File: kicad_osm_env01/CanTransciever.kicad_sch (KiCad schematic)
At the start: 24 parts

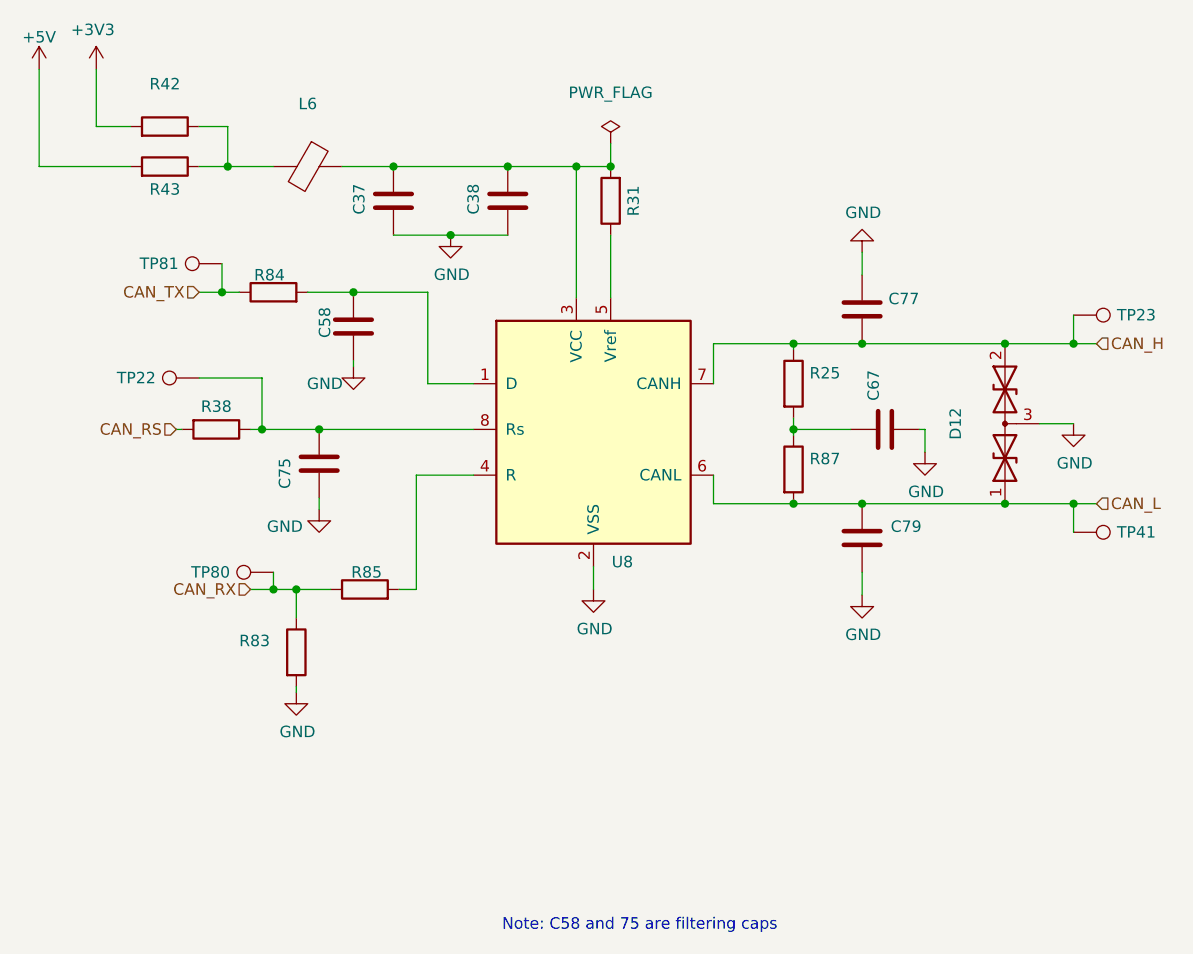
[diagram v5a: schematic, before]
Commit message: majority of signals routed on layout
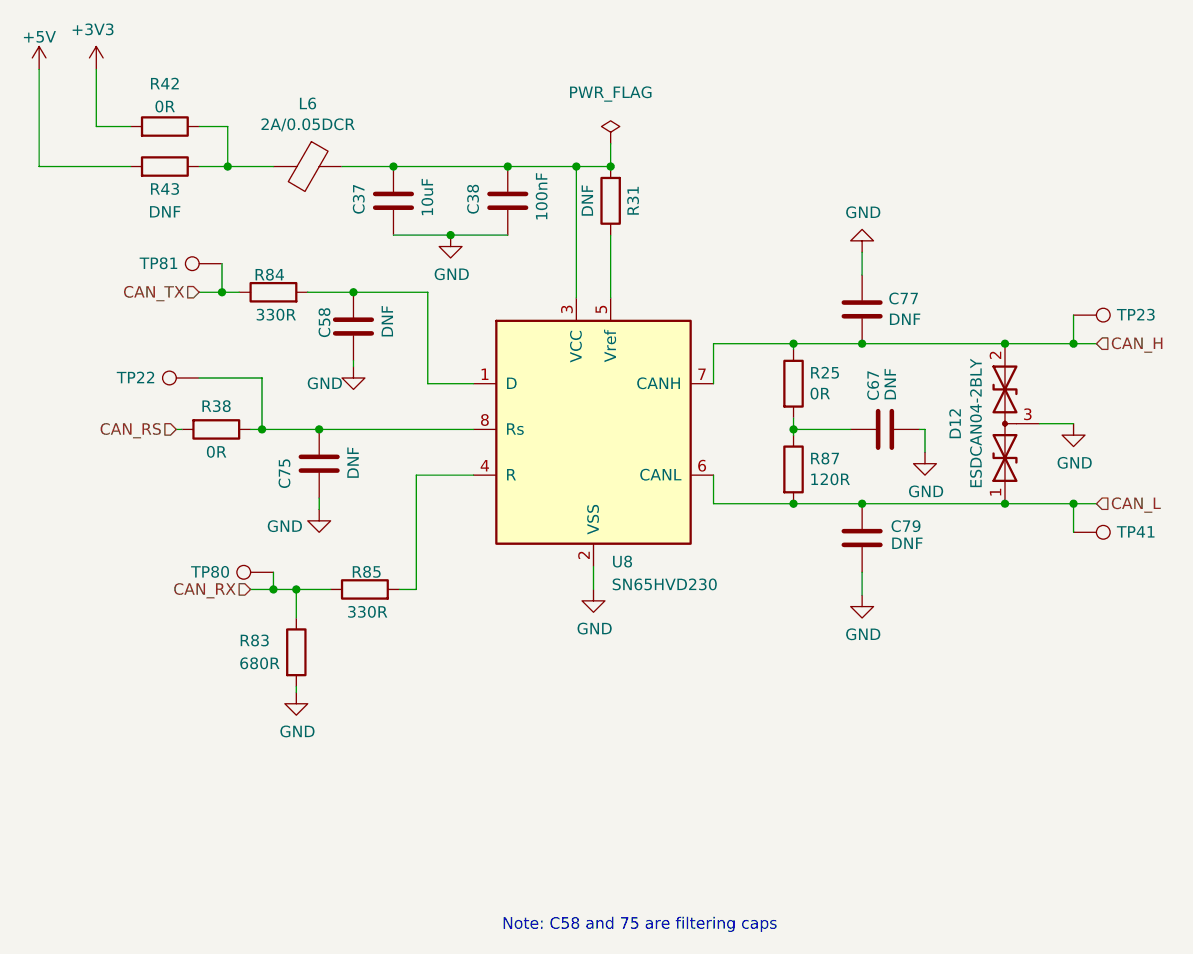
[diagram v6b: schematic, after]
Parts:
- C37: value (none) -> 10uF; footprint (none) -> Capacitor_SMD:C_0603_1608Metric
- C38: value (none) -> 100nF; footprint (none) -> Capacitor_SMD:C_0402_1005Metric
- C58, C67, C75, C77, C79: value (none) -> DNF; footprint (none) -> Capacitor_SMD:C_0603_1608Metric
- D12: value (none) -> ESDCAN04-2BLY; footprint (none) -> Package_TO_SOT_SMD:SOT-23
- L6: value (none) -> 2A/0.05DCR; footprint (none) -> Inductor_SMD:L_0402_1005Metric
- R25, R38, R42: value (none) -> 0R; footprint (none) -> Resistor_SMD:R_0603_1608Metric
- R31, R43: value (none) -> DNF; footprint (none) -> Resistor_SMD:R_0603_1608Metric
- R83: value (none) -> 680R; footprint (none) -> Resistor_SMD:R_0603_1608Metric
- R84, R85: value (none) -> 330R; footprint (none) -> Resistor_SMD:R_0603_1608Metric
- R87: value (none) -> 120R; footprint (none) -> Resistor_SMD:R_0603_1608Metric
- TP22, TP23, TP41, TP80, TP81: value (none) -> Test_Point; footprint (none) -> TestPoint:TestPoint_THTPad_D1.0mm_Drill0.5mm
- U8: value (none) -> SN65HVD230; footprint (none) -> Package_SO:SOIC-8_3.9x4.9mm_P1.27mm

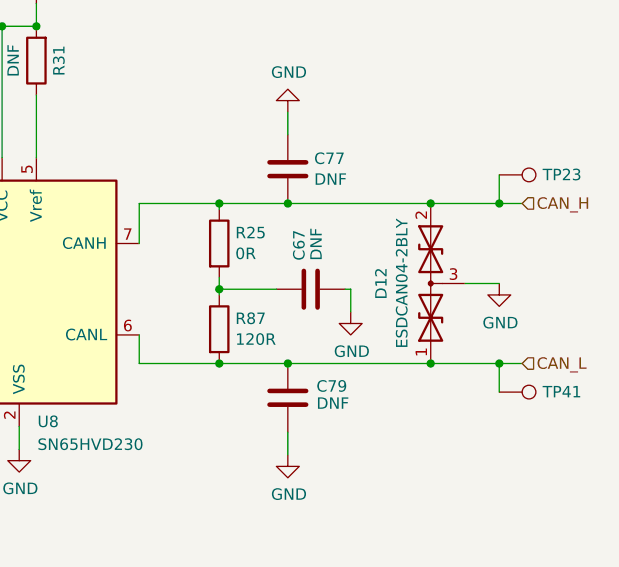
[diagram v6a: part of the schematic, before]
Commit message: updated layout
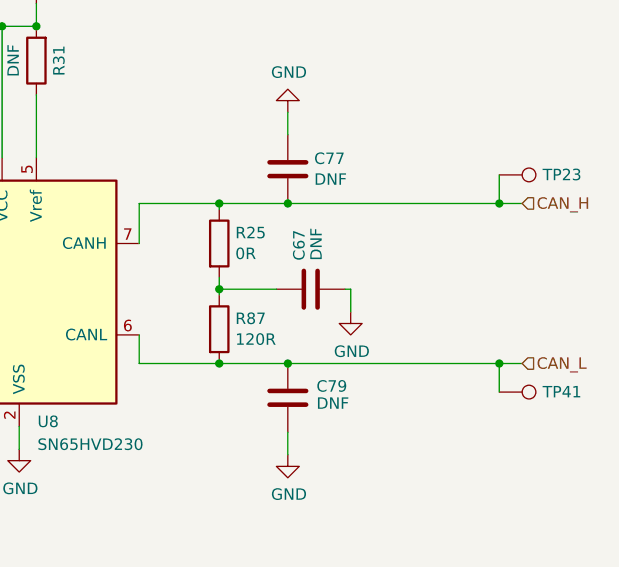
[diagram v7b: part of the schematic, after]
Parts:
- removed D12: ESDCAN04-2BLY, Package_TO_SOT_SMD:SOT-23, symbol Device:D_TVS_Dual_AAC
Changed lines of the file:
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@@
   (junction (at 112.395 72.39) (diameter 0) (color 0 0 0 0)
   )
-  (junction (at 198.755 109.855) (diameter 0) (color 0 0 0 0)
-  )
   (junction (at 154.94 72.39) (diameter 0) (color 0 0 0 0)
   )
@@
   (junction (at 182.88 109.855) (diameter 0) (color 0 0 0 0)
   )
-  (junction (at 198.755 92.075) (diameter 0) (color 0 0 0 0)
-  )
   (junction (at 126.365 86.36) (diameter 0) (color 0 0 0 0)
   )
@@
     (stroke (width 0) (type default) (color 0 0 0 0))
   )
-  (wire (pts (xy 182.88 109.855) (xy 198.755 109.855))
+  (wire (pts (xy 182.88 109.855) (xy 206.375 109.855))
     (stroke (width 0) (type default) (color 0 0 0 0))
   )
@@
     (stroke (width 0) (type default) (color 0 0 0 0))
   )
-  (wire (pts (xy 202.565 100.965) (xy 206.375 100.965))
-    (stroke (width 0) (type default) (color 0 0 0 0))
-  )
   (wire (pts (xy 126.365 94.615) (xy 126.365 93.98))
     (stroke (width 0) (type default) (color 0 0 0 0))
@@
     (stroke (width 0) (type default) (color 0 0 0 0))
   )
-  (wire (pts (xy 198.755 92.075) (xy 206.375 92.075))
-    (stroke (width 0) (type default) (color 0 0 0 0))
-  )
-  (wire (pts (xy 182.88 92.075) (xy 198.755 92.075))
+  (wire (pts (xy 182.88 92.075) (xy 206.375 92.075))
     (stroke (width 0) (type default) (color 0 0 0 0))
   )
@@
   )
   (wire (pts (xy 130.81 72.39) (xy 143.51 72.39))
-    (stroke (width 0) (type default) (color 0 0 0 0))
-  )
-  (wire (pts (xy 198.755 109.855) (xy 206.375 109.855))
     (stroke (width 0) (type default) (color 0 0 0 0))
   )
@@
     (pin "2")
   )
-  (symbol (lib_id "Device:D_TVS_Dual_AAC") (at 198.755 100.965 90) (unit 1)
-    (in_bom yes) (on_board yes)
-    (property "Reference" "D12" (id 0) (at 193.2686 100.965 0))
-    (property "Value" "ESDCAN04-2BLY " (id 1) (at 195.58 100.965 0))
-    (property "Footprint" "Package_TO_SOT_SMD:SOT-23" (id 2) (at 198.755 104.775 0)
-      (effects (font (size 1.27 1.27)) hide)
-    )
-    (property "Datasheet" "~" (id 3) (at 198.755 104.775 0)
-      (effects (font (size 1.27 1.27)) hide)
-    )
-    (pin "1")
-    (pin "2")
-    (pin "3")
-  )
   (symbol (lib_id "Device:C") (at 182.88 88.265 0) (unit 1)
     (in_bom yes) (on_board yes)
@@
       (effects (font (size 1.524 1.524)))
     )
-    (pin "1")
-  )
-  (symbol (lib_id "power:GND") (at 206.375 100.965 0) (unit 1)
-    (in_bom yes) (on_board yes)
-    (property "Reference" "#PWR0147" (id 0) (at 206.375 107.315 0)
-      (effects (font (size 1.27 1.27)) hide)
-    )
-    (property "Value" "GND" (id 1) (at 206.502 105.3592 0))
-    (property "Footprint" "" (id 2) (at 206.375 100.965 0)
-      (effects (font (size 1.524 1.524)))
-    )
-    (property "Datasheet" "" (id 3) (at 206.375 100.965 0)
-      (effects (font (size 1.524 1.524)))
-    )
